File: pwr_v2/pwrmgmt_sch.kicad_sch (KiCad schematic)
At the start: 15 parts, among them U1 LM2576S-5, U2 LM2576S-12, U3 LM2576S-3.3

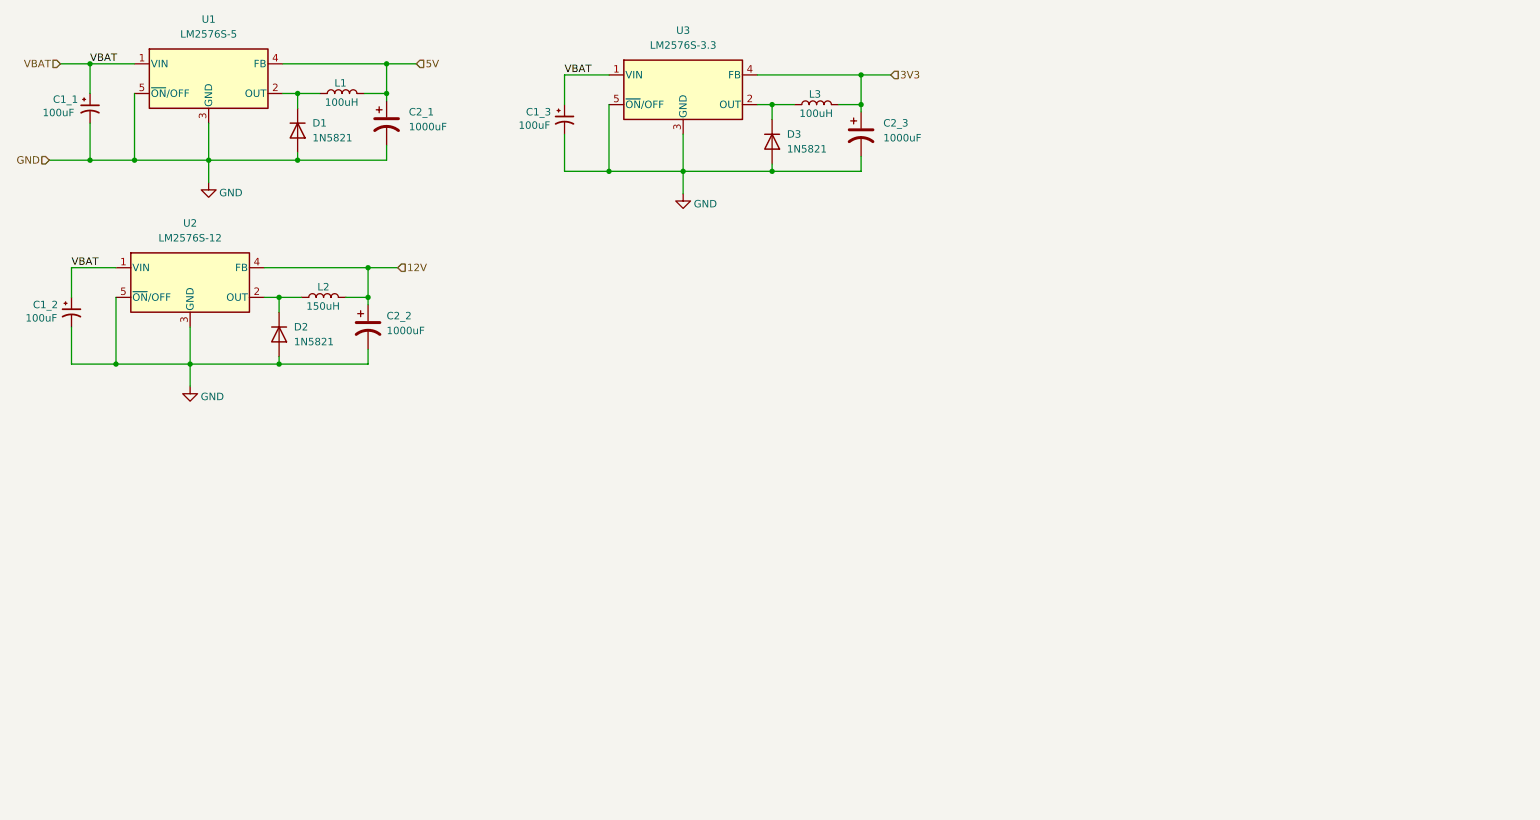
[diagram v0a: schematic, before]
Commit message: File structure enhanced.
Added uniform titleblocks and 3D renders for easier view, file cleanups.
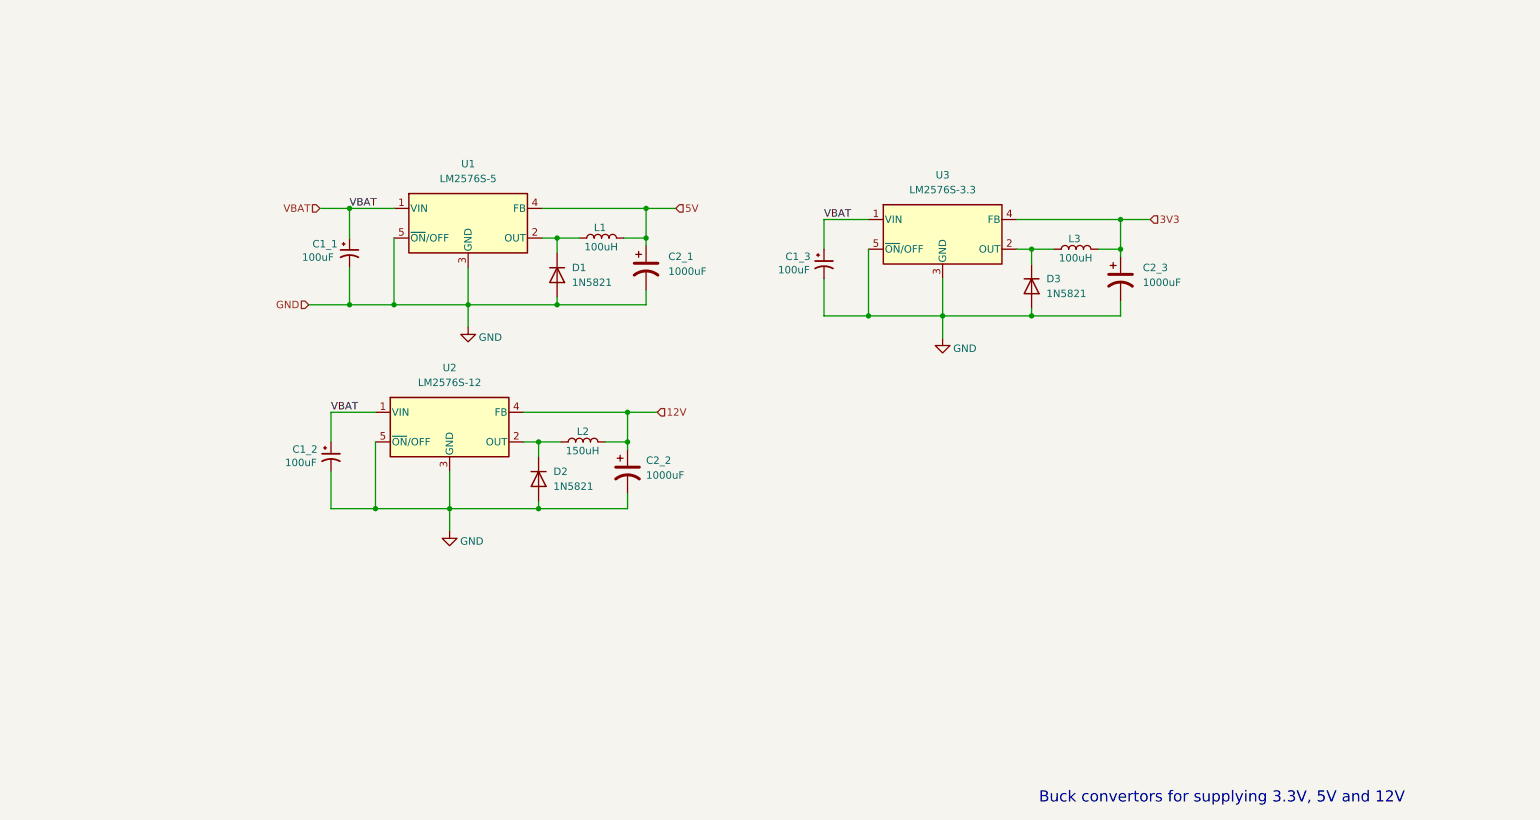
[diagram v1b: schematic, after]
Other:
- note added: "Buck convertors for supplying 3.3V, 5V and 12V"
- moved on the sheet: C1_1, C1_2, C1_3, C2_1, C2_2, C2_3, D1, D2, D3, L1, L2, L3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
